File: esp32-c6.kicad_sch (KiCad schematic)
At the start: 12 parts, among them J1 USB_C_Receptacle_USB2.0_14P, J3 Conn_02x15_Odd_Even, SW1 SW_DIP_x02, U1 ESP32-C6-MINI-1, U3 CH340N, U4 LT1963AxST-3.3

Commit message: usb-to-uart bridge change
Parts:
- removed D1, D2: 1N5711UR, Diode_SMD:D_MELF, symbol Diode:1N5711UR
- removed J3: Conn_02x15_Odd_Even, symbol Connector_Generic:Conn_02x15_Odd_Even
- removed U3: CH340N, Package_SO:JEITA_SOIC-8_3.9x4.9mm_P1.27mm, symbol Interface_USB:CH340N
- added C4: 4.7u, symbol Device:C
- added C5: 0.1u, symbol Device:C
- added D1, D2, D6, D7, D8: ESD5Zxx, Diode_SMD:D_SOD-523, symbol Diode:ESD5Zxx
- added D3: WS2812B, LED_SMD:LED_WS2812B_PLCC4_5.0x5.0mm_P3.2mm, symbol LED:WS2812B
- added D5: 1N5819WS, Diode_SMD:D_SOD-323, symbol Diode:1N5819WS
- added H1, H2, H3, H4: MountingHole, symbol Mechanical:MountingHole
- added J10: Barrel_Jack, symbol Connector:Barrel_Jack
- added J2: USB_C_Receptacle_USB2.0_14P, symbol Connector:USB_C_Receptacle_USB2.0_14P
- added J4: Conn_01x10_Socket, symbol Connector:Conn_01x10_Socket
- added J5, J6: Conn_01x08_Socket, symbol Connector:Conn_01x08_Socket
- added J7: Conn_01x06_Socket, symbol Connector:Conn_01x06_Socket
- added J8, J9: Conn_02x03_Counter_Clockwise, symbol Connector_Generic:Conn_02x03_Counter_Clockwise
- added Q1: BC847BDW1, Package_TO_SOT_SMD:SOT-363_SC-70-6, symbol Transistor_BJT:BC847BDW1
- added R2, R3, R4: 5.1k, symbol Device:R
- added R5, R7, R8, R9: 10k, symbol Device:R
- added R6: 1k, symbol Device:R
- added SW2, SW3: SW_Push, symbol Switch:SW_Push
- added U6: CP2102N-Axx-xQFN28, Package_DFN_QFN:QFN-28-1EP_5x5mm_P0.5mm_EP3.35x3.35mm, symbol Interface_USB:CP2102N-Axx-xQFN28
- C1: value 330p -> 0.1u
- C2: value 0.1u -> 10u/25V
- C3: value 330p -> 1u
- R1: value 5k -> 5.1k
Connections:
- net +3.3V: now also C4.1, C5.1, R5.1, R6.1, U6.6 (VDD), U6.7 (VREGIN); no longer C2.1
- net GND: now also C1.1, R1.2, C4.2, C5.2, D1.2 (A), D2.2 (A), D6.2 (A), D7.2 (A), D8.2 (A), J2.A1 (GND), J2.A12 (GND), J2.B1 (GND), J2.B12 (GND), J2.S1 (SHIELD), R2.2, R3.2, R4.2, R7.2, SW2.1, U6.29 (GND), U6.3 (GND); no longer C1.2
- net VBUS: no longer J1.A4 (VBUS), J1.A9 (VBUS), J1.B4 (VBUS), J1.B9 (VBUS)
- net D+_A: now reaches J1.A6 (D+), J1.B6 (D+)
- net D+_A: now also D2.1 (K), D7.1 (K), J2.A7 (D-), J2.B7 (D-), U6.4 (D+)
- net D-_A: now reaches J1.A7 (D-), J1.B7 (D-)
- net D-_A: now also D1.1 (K), D6.1 (K), J2.A6 (D+), J2.B6 (D+), U6.5 (D-)
- net at R1.1: now also J1.B5 (CC2)
- net at J1.A5 (CC1): now also R2.1; no longer C3.1
- net UART_TX: now reaches U1.30 (RXD0)
- net UART_TX: now also U6.26 (TXD)
- net UART_RX: now reaches U1.31 (TXD0)
- net UART_RX: now also U6.25 (RXD)
- net EN: now reaches U1.8 (EN)
- net EN: now also C1.2, C3.1, R5.2, SW2.2
- new net: J2.A5 (CC1), R4.1
- new net: J2.B5 (CC2), R3.1
- new net: Q1.1 (E1), R9.1
- new net: R7.1, U6.11 (~{SUSPEND})
- new net: R6.2, U6.9 (~{RST})
- new net: Q1.2 (B1), R8.2
- new net +5V: C2.1, D5.1 (K)
- new net CHIP_PU: Q1.3 (C2)
- new net DTR: Q1.5 (B2), R9.2, U6.28 (~{DTR})
- new net GPIO9: Q1.6 (C1)
- new net RTS: Q1.4 (E2), R8.1, U6.24 (~{RTS})
- new net VBUS_A: D5.2 (A), D8.1 (K), J1.A4 (VBUS), J1.A9 (VBUS), J1.B4 (VBUS), J1.B9 (VBUS), U6.8 (VBUS)
- new net VBUS_B: J2.A4 (VBUS), J2.A9 (VBUS), J2.B4 (VBUS), J2.B9 (VBUS)
- no-connect marks 0 -> 15
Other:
- moved on the sheet: R1, U1

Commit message: wroom change + boot & reset
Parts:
- removed U1: ESP32-C6-MINI-1, RF_Module:ESP32-C6-MINI-1, symbol RF_Module:ESP32-C6-MINI-1
- added C6: NC, symbol Device:C
- added C7, C9: 0.1u, symbol Device:C
- added C8: 10u, symbol Device:C
- added D4: 1N4148W, Diode_SMD:D_SOD-123, symbol Diode:1N4148W
- added R10, R11, R13, R14: 0, symbol Device:R
- added R12, R15: 10k, symbol Device:R
- added U2: ESP32-C6-WROOM-1-N8, ESP32-C6-WROOM-1-N8:XCVR_ESP32-C6-WROOM-1-N8, symbol uno-esp:ESP32-C6-WROOM-1-N8
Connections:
- net +3.3V: now also C7.1, C8.1, U2.2 (3V3)
- net +5V: now also D3.1 (VDD), R12.1
- net CHIP_PU: now also R13.1; no longer Q1.3 (C2)
- net D+_A: no longer D2.1 (K), D7.1 (K), J1.A6 (D+), J1.B6 (D+), J2.A7 (D-), J2.B7 (D-)
- net D-_A: no longer D1.1 (K), D6.1 (K), J1.A7 (D-), J1.B7 (D-), J2.A6 (D+), J2.B6 (D+)
- net DTR: now also R15.2; no longer Q1.5 (B2)
- net GND: now also D3.3 (VSS), SW3.1, C6.2, C7.2, C8.2, C9.1, U2.1 (GND), U2.28 (GND), U2.29_1 (GND), U2.29_2 (GND), U2.29_3 (GND), U2.29_4 (GND), U2.29_5 (GND), U2.29_6 (GND), U2.29_7 (GND), U2.29_8 (GND), U2.29_9 (GND)
- net GPIO9: now also SW3.2, C9.2, R10.1; no longer Q1.6 (C1)
- net UART_RX: now also U2.25 (TXD0/GPIO16)
- net UART_TX: now also U2.24 (RXD0/GPIO17)
- net at D3.4 (DIN): now also R11.1
- new net: D4.2 (A), R11.2, R12.2
- new net: Q1.5 (B2), R14.1
- new net: C6.1, R14.2, R15.1
- new net: Q1.6 (C1), R10.2
- new net: Q1.3 (C2), R13.2
- new net DA_N: D1.1 (K), J1.A7 (D-), J1.B7 (D-)
- new net DA_P: D2.1 (K), J1.A6 (D+), J1.B6 (D+)
- new net DB_N: D7.1 (K), J2.A7 (D-), J2.B7 (D-)
- new net DB_P: D6.1 (K), J2.A6 (D+), J2.B6 (D+)
- new net GPIO8: D4.1 (K)
- no-connect marks 15 -> 16
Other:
- moved on the sheet: D3, H1, H2, H3, H4, J10, J4, J5, J6, J7, J8, J9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

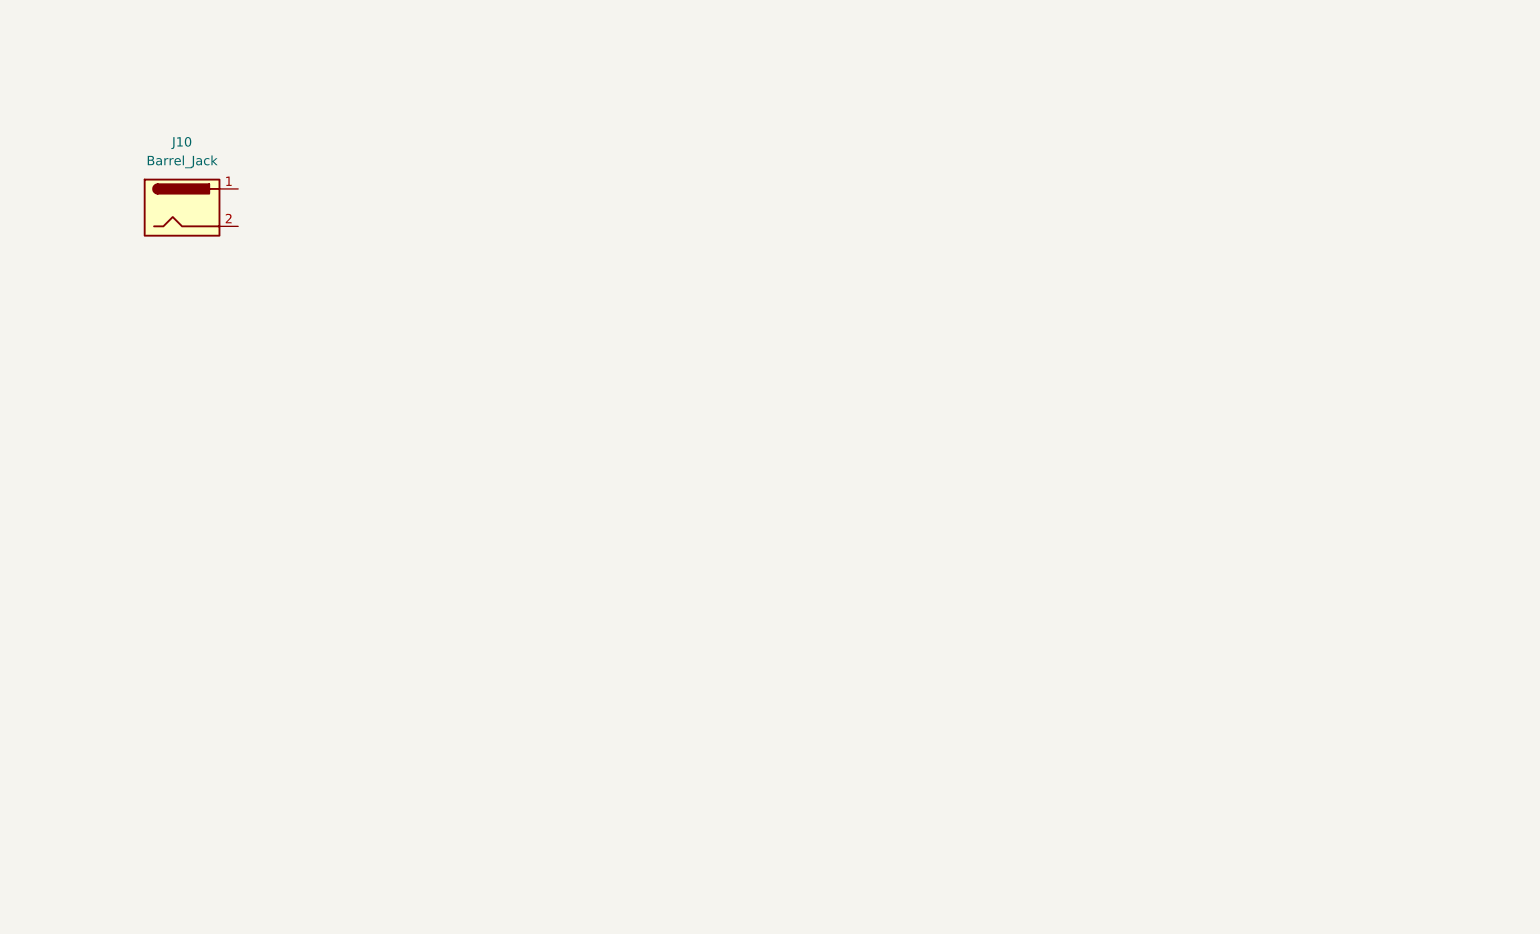
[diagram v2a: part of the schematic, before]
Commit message: barrel jack mpq9841 +
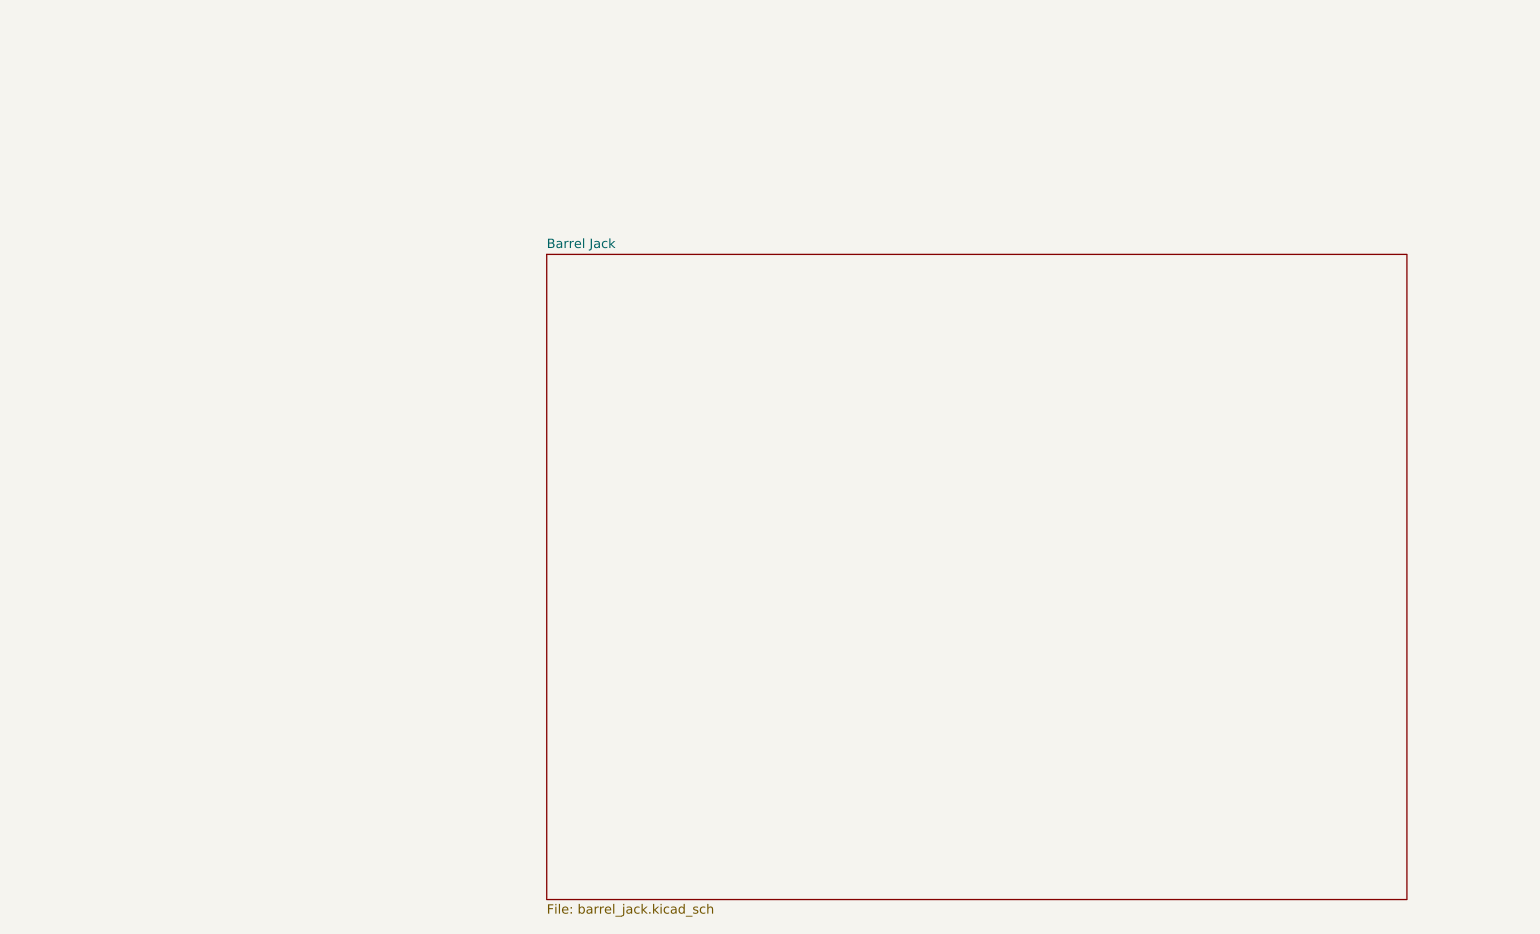
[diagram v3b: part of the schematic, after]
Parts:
- removed J10: Barrel_Jack, symbol Connector:Barrel_Jack
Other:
- added sheet Barrel Jack (barrel_jack.kicad_sch)
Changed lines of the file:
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@@
-	)
-	(symbol
-		(lib_id "Connector:Barrel_Jack")
-		(at 384.81 265.43 0)
-		(unit 1)
-		(exclude_from_sim no)
-		(in_bom yes)
-		(on_board yes)
-		(dnp no)
-		(fields_autoplaced yes)
-		(property "Reference" "J10"
-			(at 384.81 256.54 0)
-			(effects
-				(font
-					(size 1.27 1.27)
-				)
-			)
-		)
-		(property "Value" "Barrel_Jack"
-			(at 384.81 259.08 0)
-			(effects
-				(font
-					(size 1.27 1.27)
-				)
-			)
-		)
-		(property "Footprint" ""
-			(at 386.08 266.446 0)
-			(effects
-				(font
-					(size 1.27 1.27)
-				)
-				(hide yes)
-			)
-		)
-		(property "Datasheet" "~"
-			(at 386.08 266.446 0)
-			(effects
-				(font
-					(size 1.27 1.27)
-				)
-				(hide yes)
-			)
-		)
-		(property "Description" "DC Barrel Jack"
-			(at 384.81 265.43 0)
-			(effects
-				(font
-					(size 1.27 1.27)
-				)
-				(hide yes)
-			)
-		)
-		(pin "1"
-		)
-		(pin "2"
-		)
-		(instances
-			(project ""
-				(path "/98d6a3bc-4267-493f-8210-1fe038eb9de4"
-					(reference "J10")
-					(unit 1)
-				)
-			)
-		)
 	)
 	(symbol
@@
 				)
 			)
+		)
+	)
+	(sheet
+		(at 434.34 271.78)
+		(size 116.84 87.63)
+		(exclude_from_sim no)
+		(in_bom yes)
+		(on_board yes)
+		(dnp no)
+		(fields_autoplaced yes)
+		(stroke
+			(width 0.1524)
+			(type solid)
+		)
+		(fill
+			(color 0 0 0 0.0000)
+		)
+		(property "Sheetname" "Barrel Jack"
+			(at 434.34 271.0684 0)
+			(effects
+				(font
+					(size 1.27 1.27)
+				)
+				(justify left bottom)
+			)
+		)
+		(property "Sheetfile" "barrel_jack.kicad_sch"
+			(at 434.34 359.9946 0)
+			(effects
+				(font
+					(size 1.27 1.27)
+				)
+				(justify left top)
+			)
+		)
+		(instances
+			(project "esp32-c6"
+				(path "/98d6a3bc-4267-493f-8210-1fe038eb9de4"
+					(page "2")
+				)
+			)

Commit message: NCP1117-3.3 change
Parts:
- removed U4: LT1963AxST-3.3, Package_TO_SOT_SMD:SOT-223-3_TabPin2, symbol Regulator_Linear:LT1963AxST-3.3
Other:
- moved on the sheet: C7, C8, H1, H2, H3, H4, J4, J5, J6, J7, J8, J9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

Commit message: header pins + footprint assignment
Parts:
- removed C7: 0.1u, symbol Device:C
- removed C8: 10u, symbol Device:C
- removed H1, H2, H3, H4: MountingHole, symbol Mechanical:MountingHole
- removed J4: Conn_01x10_Socket, symbol Connector:Conn_01x10_Socket
- removed J5, J6: Conn_01x08_Socket, symbol Connector:Conn_01x08_Socket
- removed J7: Conn_01x06_Socket, symbol Connector:Conn_01x06_Socket
- removed J8, J9: Conn_02x03_Counter_Clockwise, symbol Connector_Generic:Conn_02x03_Counter_Clockwise
- removed SW1: SW_DIP_x02, symbol Switch:SW_DIP_x02
- removed U2: ESP32-C6-WROOM-1-N8, ESP32-C6-WROOM-1-N8:XCVR_ESP32-C6-WROOM-1-N8, symbol uno-esp:ESP32-C6-WROOM-1-N8
- C1: renamed from C2; footprint (none) -> Capacitor_SMD:C_0603_1608Metric
- C3: renamed from C4; footprint (none) -> Capacitor_SMD:C_0201_0603Metric
- C4: renamed from C5; footprint (none) -> Capacitor_SMD:C_0201_0603Metric
- C5: renamed from C9; footprint (none) -> Capacitor_SMD:C_0201_0603Metric
- C6: renamed from C1; footprint (none) -> Capacitor_SMD:C_0201_0603Metric
- C7: renamed from C3; footprint (none) -> Capacitor_SMD:C_0402_1005Metric
- J1, J2: footprint (none) -> Connector_USB:USB_C_Receptacle_GCT_USB4105-xx-A_16P_TopMnt_Horizontal
- R1, R4, R9: footprint (none) -> Resistor_SMD:R_0402_1005Metric
- R10: renamed from R8; footprint (none) -> Resistor_SMD:R_0402_1005Metric
- R11: renamed from R15; footprint (none) -> Resistor_SMD:R_0201_0603Metric_Pad0.64x0.40mm_HandSolder
- R12: renamed from R14; footprint (none) -> Resistor_SMD:R_0201_0603Metric
- R13: footprint (none) -> Resistor_SMD:R_0201_0603Metric
- R14: renamed from R7; footprint (none) -> Resistor_SMD:R_0402_1005Metric
- R15: renamed from R5; footprint (none) -> Resistor_SMD:R_0402_1005Metric
- R2: renamed from R3; footprint (none) -> Resistor_SMD:R_0402_1005Metric
- R3: renamed from R2; footprint (none) -> Resistor_SMD:R_0402_1005Metric
- R5: renamed from R12; footprint (none) -> Resistor_SMD:R_0402_1005Metric
- R6: renamed from R11; footprint (none) -> Resistor_SMD:R_0201_0603Metric
- R7: renamed from R6; footprint (none) -> Resistor_SMD:R_0402_1005Metric
- R8: renamed from R10; footprint (none) -> Resistor_SMD:R_0201_0603Metric
- SW1: renamed from SW3; footprint (none) -> Button_Switch_SMD:SW_SPST_TS-1088-xR020
- SW2: footprint (none) -> Button_Switch_SMD:SW_SPST_TS-1088-xR020
- renumbered C6 to C2, D6 to D1, D8 to D2, D2 to D3, D7 to D4, D1 to D5, D5 to D6, D4 to D7, D3 to D8, U6 to U1
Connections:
- net DB_N renamed IO12_DB_N
- net DB_P renamed IO13_DB_P
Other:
- added sheet esp32-c6 Pinout (c6_pinout.kicad_sch)
- moved on the sheet: C6, C7, R15, SW2

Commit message: pcb component layout
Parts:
- added D13: ESD5Zxx, Diode_SMD:D_SOD-523, symbol Diode:ESD5Zxx
- added D14: 1N5819WS, Diode_SMD:D_SOD-323, symbol Diode:1N5819WS
- C2: value NC -> 10u/25V; footprint (none) -> Capacitor_SMD:C_0603_1608Metric
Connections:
- net +5V: now also C2.1, D14.1 (K)
- net GND: now also R11.1, R12.2, D13.2 (A)
- net VBUS_B: now also D13.1 (K), D14.2 (A)
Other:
- moved on the sheet: C6, C7, R15, R7, SW2
